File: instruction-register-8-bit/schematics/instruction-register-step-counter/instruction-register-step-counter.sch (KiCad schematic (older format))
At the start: 15 parts

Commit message: small corrections to design
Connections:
- net CLK: no longer U?.2 (CP)
- new net ~CLK: U?.2 (CP)
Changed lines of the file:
@@
 IRi
-Wire Wire Line
-	9825 2300 8675 2300
 Wire Wire Line
 	9825 2500 8575 2500
@@
 Connection ~ 4950 3475
 Wire Wire Line
-	8675 2300 8675 1900
-Wire Wire Line
-	8675 1900 5825 1900
-Wire Wire Line
-	5825 1900 5825 3200
+	8650 1975 5825 1975
+Wire Wire Line
+	5825 1975 5825 3200
 Wire Wire Line
 	5825 3200 4750 3200
 Wire Wire Line
 	4750 3200 4750 3600
-Connection ~ 8675 2300
-Wire Wire Line
-	8675 2300 8575 2300
 $Comp
 L power:GND #PWR?
@@
 	7875 1700 7875 3600
 Connection ~ 2425 1700
+Wire Wire Line
+	8575 2300 9825 2300
+Text HLabel 9825 2100 2    50   Input ~ 0
+~CLK
+Wire Wire Line
+	9825 2100 8650 2100
+Wire Wire Line
+	8650 2100 8650 1975
 $EndSCHEMATC

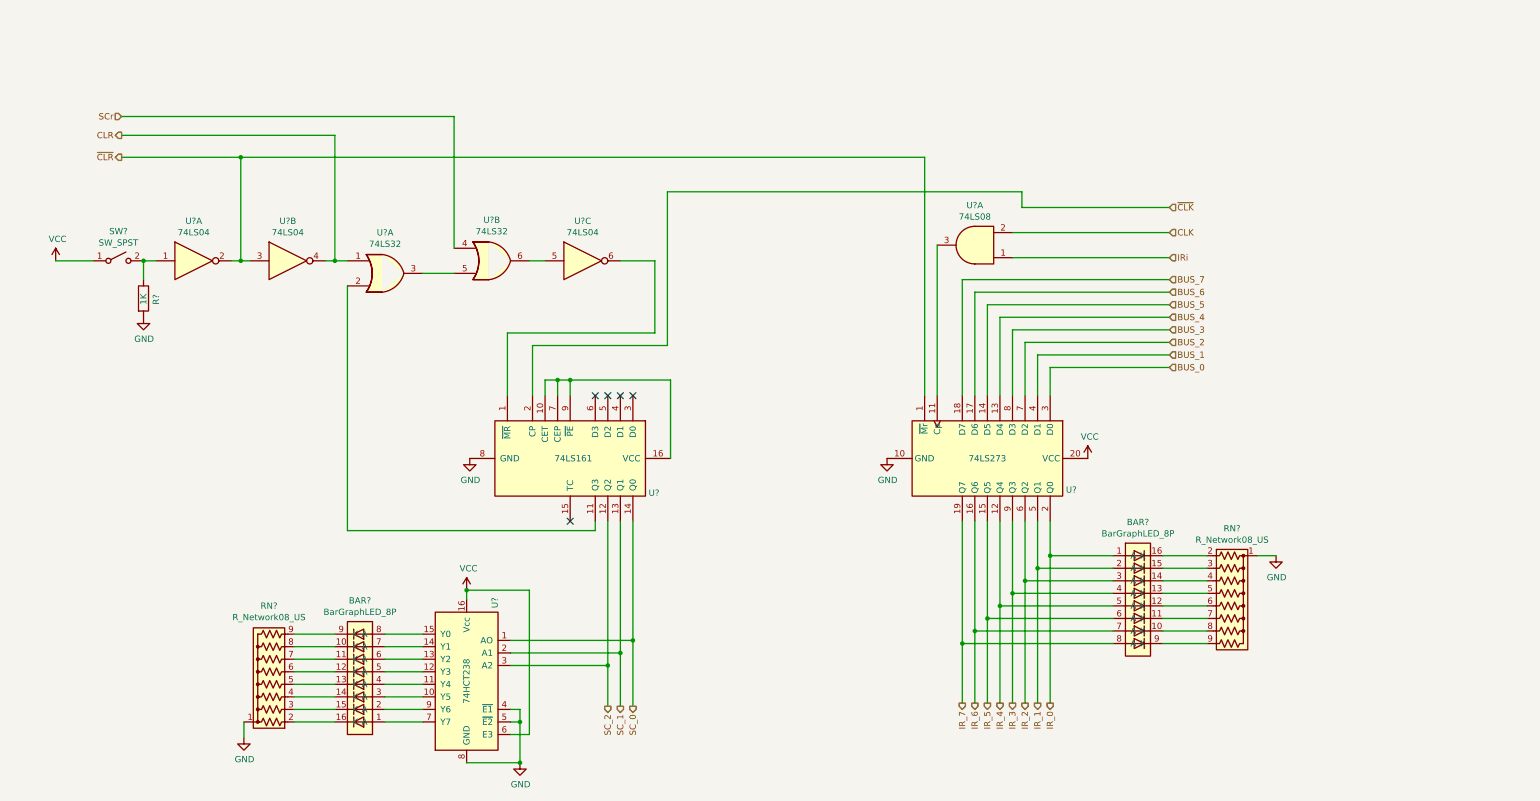
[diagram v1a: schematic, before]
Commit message: updated register design to enable extended instructions
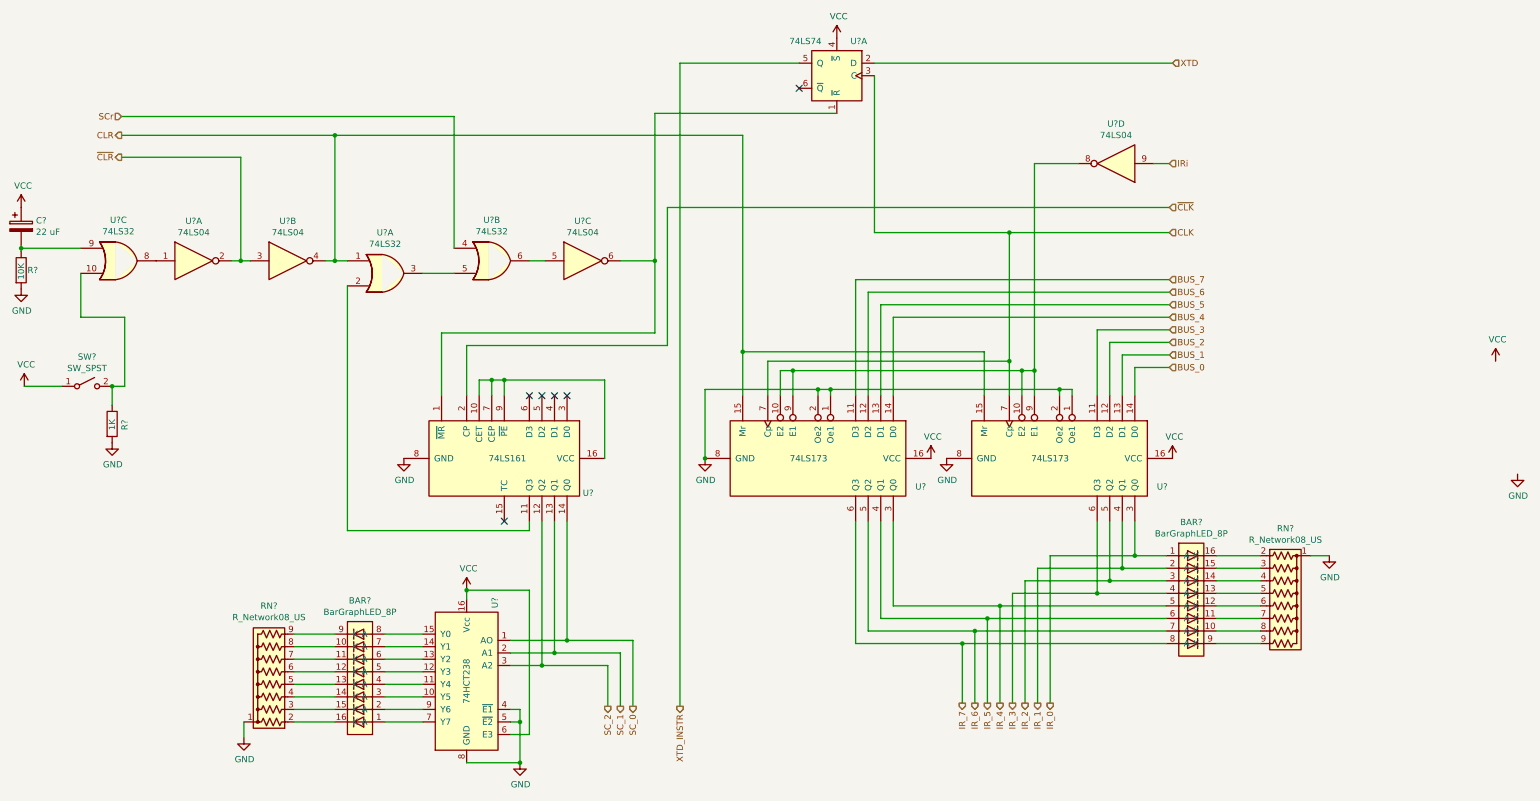
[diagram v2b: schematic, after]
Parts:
- removed U?: 74LS273, symbol 74xx:74LS273
- removed U?: 74LS08, symbol 74xx:74LS08
- added C?: 22 uF, symbol Device:CP
- added R?: 10K, symbol Device:R
- added U? (x2): 74LS173, symbol 74xx:74LS173
- added U?: 74LS74, symbol 74xx:74LS74
- added U?: 74LS04, symbol 74xx:74LS04
- added U?: 74LS32, symbol 74xx:74LS32
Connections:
- net BUS_0: now also U?.14 (D0)
- net BUS_1: now also U?.13 (D1)
- net BUS_2: now also U?.12 (D2)
- net BUS_3: now also U?.11 (D3)
- net BUS_4: now also U?.14 (D0)
- net BUS_5: now also U?.13 (D1)
- net BUS_6: now also U?.12 (D2)
- net BUS_7: now also U?.11 (D3)
- net CLK: now also U?.3 (C), U?.7 (Cp), U?.7 (Cp)
- net CLR: now also U?.15 (Mr), U?.15 (Mr)
- net GND: now also R?.2, U?.1 (Oe1), U?.1 (Oe1), U?.2 (Oe2), U?.2 (Oe2), U?.8 (GND), U?.8 (GND)
- net IR_0: now also U?.3 (Q0)
- net IR_1: now also U?.4 (Q1)
- net IR_2: now also U?.5 (Q2)
- net IR_3: now also U?.6 (Q3)
- net IR_4: now also U?.3 (Q0)
- net IR_5: now also U?.4 (Q1)
- net IR_6: now also U?.5 (Q2)
- net IR_7: now also U?.6 (Q3)
- net IRi: now also U?.9
- net VCC: now also C?.1, U?.16 (VCC), U?.16 (VCC), U?.4 (~S)
- net at U?.1 (~MR), U?.6: now also U?.1 (~R)
- net at R?.1, SW?.2 (B): now also U?.10; no longer U?.1
- new net: U?.1, U?.8
- new net: U?.10 (E2), U?.10 (E2), U?.8, U?.9 (E1), U?.9 (E1)
- new net: C?.2, R?.1, U?.9
- new net XTD: U?.2 (D)
- new net XTD_INSTR: U?.5 (Q)
- no-connect marks 5 -> 6
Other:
- moved on the sheet: BAR?, R?, RN?, SW?, U?

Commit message: candidate final schematic designs
Also started to consolidate custom symbols from all projects
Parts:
- BAR? (x2): symbol instruction-register-symbols:BarGraphLED_8P -> common-symbols:BarGraphLED_8P
- U?: symbol instruction-register-symbols:74HCT238 -> common-symbols:74HCT238
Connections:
- net INSTR_RESET: now reaches U?.5, U?.6
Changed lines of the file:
@@
 IR_7
 $Comp
-L instruction-register-symbols:BarGraphLED_8P BAR?
+L common-symbols:BarGraphLED_8P BAR?
 U 1 1 60CF32C9
 P 10000 5275
@@
 $EndComp
 $Comp
-L instruction-register-symbols:74HCT238 U?
-U 1 1 60D24130
-P 4225 5850
-F 0 "U?" V 4000 6450 50  0000 C CNN
-F 1 "74HCT238" V 4225 5825 50  0000 C CNN
-F 2 "" H 4075 5675 50  0001 C CNN
-F 3 "" H 4075 5675 50  0001 C CNN
-	1    4225 5850
-	-1   0    0    -1
-$EndComp
-$Comp
 L Switch:SW_SPST SW?
 U 1 1 60D2779C
@@
 	5350 5750 5350 6075
 $Comp
-L instruction-register-symbols:BarGraphLED_8P BAR?
+L common-symbols:BarGraphLED_8P BAR?
 U 1 1 60D969A0
 P 3375 5800
@@
 Wire Wire Line
 	2450 6325 2450 6200
-$Comp
-L power:GND #PWR?
-U 1 1 60DE01F3
-P 12600 4225
-F 0 "#PWR?" H 12600 3975 50  0001 C CNN
-F 1 "GND" H 12605 4052 50  0000 C CNN
-F 2 "" H 12600 4225 50  0001 C CNN
-F 3 "" H 12600 4225 50  0001 C CNN
-	1    12600 4225
-	1    0    0    -1
-$EndComp
-$Comp
-L power:VCC #PWR?
-U 1 1 60DE082D
-P 12425 3325
-F 0 "#PWR?" H 12425 3175 50  0001 C CNN
-F 1 "VCC" H 12440 3498 50  0000 C CNN
-F 2 "" H 12425 3325 50  0001 C CNN
-F 3 "" H 12425 3325 50  0001 C CNN
-	1    12425 3325
-	1    0    0    -1
-$EndComp
 Wire Wire Line
 	4575 6200 4650 6200
@@
 $EndComp
 Wire Wire Line
-	4725 2525 4850 2525
+	4725 2525 4775 2525
 Wire Wire Line
 	5725 2525 5725 1350
@@
 Text HLabel 5925 6075 3    50   Output ~ 0
 XTD_INSTR
+$Comp
+L common-symbols:74HCT238 U?
+U 1 1 60D24130
+P 4225 5850
+F 0 "U?" V 4000 6450 50  0000 C CNN
+F 1 "74HCT238" V 4225 5825 50  0000 C CNN
+F 2 "" H 4075 5675 50  0001 C CNN
+F 3 "" H 4075 5675 50  0001 C CNN
+	1    4225 5850
+	-1   0    0    -1
+$EndComp
+Wire Wire Line
+	4775 2525 4775 1225
+Wire Wire Line
+	4775 1225 1475 1225
+Connection ~ 4775 2525
+Wire Wire Line
+	4775 2525 4850 2525
+Text HLabel 1475 1225 0    50   Output ~ 0
+INSTR_RESET
 $EndSCHEMATC

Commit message: removed A16 address line
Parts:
- gave numbers to parts that had none: 15
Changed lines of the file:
@@
 IR_7
 $Comp
-L common-symbols:BarGraphLED_8P BAR?
+L common-symbols:BarGraphLED_8P BAR2
 U 1 1 60CF32C9
 P 10000 5275
-F 0 "BAR?" H 10000 5942 50  0000 C CNN
+F 0 "BAR2" H 10000 5942 50  0000 C CNN
 F 1 "BarGraphLED_8P" H 10000 5851 50  0000 C CNN
 F 2 "" H 10000 5275 50  0001 C CNN
@@
 	8175 5575 8175 6050
 $Comp
-L Device:R_Network08_US RN?
+L Device:R_Network08_US RN2
 U 1 1 60CFC0D8
 P 10750 5275
-F 0 "RN?" V 10133 5275 50  0000 C CNN
+F 0 "RN2" V 10133 5275 50  0000 C CNN
 F 1 "R_Network08_US" V 10224 5275 50  0000 C CNN
 F 2 "Resistor_THT:R_Array_SIP9" V 11225 5275 50  0001 C CNN
@@
 	10200 5575 10550 5575
 $Comp
-L power:GND #PWR?
+L power:GND #PWR014
 U 1 1 60D0AFC0
 P 11100 4875
-F 0 "#PWR?" H 11100 4625 50  0001 C CNN
+F 0 "#PWR014" H 11100 4625 50  0001 C CNN
 F 1 "GND" H 11105 4702 50  0000 C CNN
 F 2 "" H 11100 4875 50  0001 C CNN
@@
 IRi
 $Comp
-L 74xx:74LS161 U?
+L 74xx:74LS161 U4
 U 1 1 60D1A6A2
 P 4525 4100
-F 0 "U?" V 4800 4725 50  0000 L CNN
+F 0 "U4" V 4800 4725 50  0000 L CNN
 F 1 "74LS161" V 4525 3975 50  0000 L CNN
 F 2 "" H 4525 4100 50  0001 C CNN
@@
 $EndComp
 $Comp
-L Switch:SW_SPST SW?
+L Switch:SW_SPST SW1
 U 1 1 60D2779C
 P 1200 3525
-F 0 "SW?" H 1200 3760 50  0000 C CNN
+F 0 "SW1" H 1200 3760 50  0000 C CNN
 F 1 "SW_SPST" H 1200 3669 50  0000 C CNN
 F 2 "" H 1200 3525 50  0001 C CNN
@@
 $EndComp
 $Comp
-L power:VCC #PWR?
+L power:VCC #PWR03
 U 1 1 60D28594
 P 700 3525
-F 0 "#PWR?" H 700 3375 50  0001 C CNN
+F 0 "#PWR03" H 700 3375 50  0001 C CNN
 F 1 "VCC" H 715 3698 50  0000 C CNN
 F 2 "" H 700 3525 50  0001 C CNN
@@
 $EndComp
 $Comp
-L Device:R R?
+L Device:R R2
 U 1 1 60D2896A
 P 1400 3825
-F 0 "R?" V 1500 3775 50  0000 L CNN
+F 0 "R2" V 1500 3775 50  0000 L CNN
 F 1 "1K" V 1400 3775 50  0000 L CNN
 F 2 "" V 1330 3825 50  0001 C CNN
@@
 $EndComp
 $Comp
-L power:GND #PWR?
+L power:GND #PWR04
 U 1 1 60D29CBD
 P 1400 3975
-F 0 "#PWR?" H 1400 3725 50  0001 C CNN
+F 0 "#PWR04" H 1400 3725 50  0001 C CNN
 F 1 "GND" H 1405 3802 50  0000 C CNN
 F 2 "" H 1400 3975 50  0001 C CNN
@@
 	700  3525 1000 3525
 $Comp
-L 74xx:74LS04 U?
+L 74xx:74LS04 U2
 U 1 1 60D2C869
 P 2050 2525
-F 0 "U?" H 2050 2842 50  0000 C CNN
+F 0 "U2" H 2050 2842 50  0000 C CNN
 F 1 "74LS04" H 2050 2751 50  0000 C CNN
 F 2 "" H 2050 2525 50  0001 C CNN
@@
 $EndComp
 $Comp
-L 74xx:74LS32 U?
+L 74xx:74LS32 U1
 U 1 1 60D2EF1E
 P 3575 2625
-F 0 "U?" H 3575 2950 50  0000 C CNN
+F 0 "U1" H 3575 2950 50  0000 C CNN
 F 1 "74LS32" H 3575 2859 50  0000 C CNN
 F 2 "" H 3575 2625 50  0001 C CNN
@@
 $EndComp
 $Comp
-L 74xx:74LS04 U?
+L 74xx:74LS04 U2
 U 2 1 60D358DC
 P 2800 2525
-F 0 "U?" H 2800 2842 50  0000 C CNN
+F 0 "U2" H 2800 2842 50  0000 C CNN
 F 1 "74LS04" H 2800 2751 50  0000 C CNN
 F 2 "" H 2800 2525 50  0001 C CNN
@@
 NoConn ~ 4525 4600
 $Comp
-L 74xx:74LS32 U?
+L 74xx:74LS32 U1
 U 2 1 60D49D1D
 P 4425 2525
-F 0 "U?" H 4425 2850 50  0000 C CNN
+F 0 "U1" H 4425 2850 50  0000 C CNN
 F 1 "74LS32" H 4425 2759 50  0000 C CNN
 F 2 "" H 4425 2525 50  0001 C CNN
@@
 	3875 2625 4125 2625
 $Comp
-L 74xx:74LS04 U?
+L 74xx:74LS04 U2
 U 3 1 60D4E826
 P 5150 2525
-F 0 "U?" H 5150 2842 50  0000 C CNN
+F 0 "U2" H 5150 2842 50  0000 C CNN
 F 1 "74LS04" H 5150 2751 50  0000 C CNN
 F 2 "" H 5150 2525 50  0001 C CNN
@@
 	4225 3200 4225 3600
 $Comp
-L power:GND #PWR?
+L power:GND #PWR06
 U 1 1 60D63CEC
 P 3725 4100
-F 0 "#PWR?" H 3725 3850 50  0001 C CNN
+F 0 "#PWR06" H 3725 3850 50  0001 C CNN
 F 1 "GND" H 3730 3927 50  0000 C CNN
 F 2 "" H 3725 4100 50  0001 C CNN
@@
 	5350 5750 5350 6075
 $Comp
-L common-symbols:BarGraphLED_8P BAR?
+L common-symbols:BarGraphLED_8P BAR1
 U 1 1 60D969A0
 P 3375 5800
-F 0 "BAR?" H 3375 5233 50  0000 C CNN
+F 0 "BAR1" H 3375 5233 50  0000 C CNN
 F 1 "BarGraphLED_8P" H 3375 5324 50  0000 C CNN
 F 2 "" H 3375 5800 50  0001 C CNN
@@
 	3575 6200 3875 6200
 $Comp
-L Device:R_Network08_US RN?
+L Device:R_Network08_US RN1
 U 1 1 60DB642E
 P 2650 5800
-F 0 "RN?" V 3175 5800 50  0000 C CNN
+F 0 "RN1" V 3175 5800 50  0000 C CNN
 F 1 "R_Network08_US" V 3084 5800 50  0000 C CNN
 F 2 "Resistor_THT:R_Array_SIP9" V 3125 5800 50  0001 C CNN
@@
 	2850 6200 3175 6200
 $Comp
-L power:GND #PWR?
+L power:GND #PWR05
 U 1 1 60DDAC2E
 P 2450 6325
-F 0 "#PWR?" H 2450 6075 50  0001 C CNN
+F 0 "#PWR05" H 2450 6075 50  0001 C CNN
 F 1 "GND" H 2455 6152 50  0000 C CNN
 F 2 "" H 2450 6325 50  0001 C CNN
@@
 	4225 5150 4225 5225
 $Comp
-L power:VCC #PWR?
+L power:VCC #PWR07
 U 1 1 60DEFCE4
 P 4225 5150
-F 0 "#PWR?" H 4225 5000 50  0001 C CNN
+F 0 "#PWR07" H 4225 5000 50  0001 C CNN
 F 1 "VCC" H 4240 5323 50  0000 C CNN
 F 2 "" H 4225 5150 50  0001 C CNN
@@
 Connection ~ 4225 5150
 $Comp
-L power:GND #PWR?
+L power:GND #PWR08
 U 1 1 60DF031A
 P 4650 6525
-F 0 "#PWR?" H 4650 6275 50  0001 C CNN
+F 0 "#PWR08" H 4650 6275 50  0001 C CNN
 F 1 "GND" H 4655 6352 50  0000 C CNN
 F 2 "" H 4650 6525 50  0001 C CNN
@@
 ~CLK
 $Comp
-L 74xx:74LS173 U?
+L 74xx:74LS173 U7
 U 1 1 60E06F1E
 P 8950 4100
-F 0 "U?" V 9175 4875 50  0000 L CNN
+F 0 "U7" V 9175 4875 50  0000 L CNN
 F 1 "74LS173" V 8950 3875 50  0000 L CNN
 F 2 "" H 8950 4100 50  0001 C CNN
@@
 $EndComp
 $Comp
-L 74xx:74LS173 U?
+L 74xx:74LS173 U5
 U 1 1 60E0D0CC
 P 7025 4100
-F 0 "U?" V 7250 4875 50  0000 L CNN
+F 0 "U5" V 7250 4875 50  0000 L CNN
 F 1 "74LS173" V 7025 3875 50  0000 L CNN
 F 2 "" H 7025 4100 50  0001 C CNN
@@
 Connection ~ 6425 3250
 $Comp
-L 74xx:74LS04 U?
+L 74xx:74LS04 U2
 U 4 1 60EAE619
 P 9400 1750
-F 0 "U?" H 9400 1433 50  0000 C CNN
+F 0 "U2" H 9400 1433 50  0000 C CNN
 F 1 "74LS04" H 9400 1524 50  0000 C CNN
 F 2 "" H 9400 1750 50  0001 C CNN
@@
 	7125 3550 8950 3550
 $Comp
-L power:GND #PWR?
+L power:GND #PWR09
 U 1 1 60F24388
 P 6125 4100
-F 0 "#PWR?" H 6125 3850 50  0001 C CNN
+F 0 "#PWR09" H 6125 3850 50  0001 C CNN
 F 1 "GND" H 6130 3927 50  0000 C CNN
 F 2 "" H 6125 4100 50  0001 C CNN
@@
 Connection ~ 6125 4100
 $Comp
-L power:GND #PWR?
+L power:GND #PWR012
 U 1 1 60F2496F
 P 8050 4100
-F 0 "#PWR?" H 8050 3850 50  0001 C CNN
+F 0 "#PWR012" H 8050 3850 50  0001 C CNN
 F 1 "GND" H 8055 3927 50  0000 C CNN
 F 2 "" H 8050 4100 50  0001 C CNN
@@
 $EndComp
 $Comp
-L power:VCC #PWR?
+L power:VCC #PWR011
 U 1 1 60F2510D
 P 7925 4100
-F 0 "#PWR?" H 7925 3950 50  0001 C CNN
+F 0 "#PWR011" H 7925 3950 50  0001 C CNN
 F 1 "VCC" H 7940 4273 50  0000 C CNN
 F 2 "" H 7925 4100 50  0001 C CNN
@@
 $EndComp
 $Comp
-L power:VCC #PWR?
+L power:VCC #PWR013
 U 1 1 60F2574C
 P 9850 4100
-F 0 "#PWR?" H 9850 3950 50  0001 C CNN
+F 0 "#PWR013" H 9850 3950 50  0001 C CNN
 F 1 "VCC" H 9865 4273 50  0000 C CNN
 F 2 "" H 9850 4100 50  0001 C CNN
@@
 $EndComp
 $Comp
-L 74xx:74LS32 U?
+L 74xx:74LS32 U1
 U 3 1 60F2D71D
 P 1450 2525
-F 0 "U?" H 1450 2850 50  0000 C CNN
+F 0 "U1" H 1450 2850 50  0000 C CNN
 F 1 "74LS32" H 1450 2759 50  0000 C CNN
 F 2 "" H 1450 2525 50  0001 C CNN
@@
 $EndComp
 $Comp
-L Device:CP C?
+L Device:CP C1
 U 1 1 60F309C4
 P 675 2250
-F 0 "C?" H 793 2296 50  0000 L CNN
+F 0 "C1" H 793 2296 50  0000 L CNN
 F 1 "22 uF" H 793 2205 50  0000 L CNN
 F 2 "" H 713 2100 50  0001 C CNN
@@
 $EndComp
 $Comp
-L Device:R R?
+L Device:R R1
 U 1 1 60F33076
 P 675 2600
-F 0 "R?" H 725 2600 50  0000 L CNN
+F 0 "R1" H 725 2600 50  0000 L CNN
 F 1 "10K" V 675 2525 50  0000 L CNN
 F 2 "" V 605 2600 50  0001 C CNN
@@
 	675  2425 675  2450
 $Comp
-L power:VCC #PWR?
+L power:VCC #PWR01
 U 1 1 60F48D9E
 P 675 2100
-F 0 "#PWR?" H 675 1950 50  0001 C CNN
+F 0 "#PWR01" H 675 1950 50  0001 C CNN
 F 1 "VCC" H 690 2273 50  0000 C CNN
 F 2 "" H 675 2100 50  0001 C CNN
@@
 $EndComp
 $Comp
-L power:GND #PWR?
+L power:GND #PWR02
 U 1 1 60F494BC
 P 675 2750
-F 0 "#PWR?" H 675 2500 50  0001 C CNN
+F 0 "#PWR02" H 675 2500 50  0001 C CNN
 F 1 "GND" H 680 2577 50  0000 C CNN
 F 2 "" H 675 2750 50  0001 C CNN
@@
 	4025 3100 5725 3100
 $Comp
-L 74xx:74LS74 U?
+L 74xx:74LS74 U6
 U 1 1 60E828E3
 P 7175 1050
-F 0 "U?" H 7000 1325 50  0000 C CNN
+F 0 "U6" H 7000 1325 50  0000 C CNN
 F 1 "74LS74" H 7425 1325 50  0000 C CNN
 F 2 "" H 7175 1050 50  0001 C CNN
@@
 NoConn ~ 6875 1150
 $Comp
-L power:VCC #PWR?
+L power:VCC #PWR010
 U 1 1 60EFFFD1
 P 7175 750
-F 0 "#PWR?" H 7175 600 50  0001 C CNN
+F 0 "#PWR010" H 7175 600 50  0001 C CNN
 F 1 "VCC" H 7190 923 50  0000 C CNN
 F 2 "" H 7175 750 50  0001 C CNN
@@
 XTD_INSTR
 $Comp
-L common-symbols:74HCT238 U?
+L common-symbols:74HCT238 U3
 U 1 1 60D24130
 P 4225 5850
-F 0 "U?" V 4000 6450 50  0000 C CNN
+F 0 "U3" V 4000 6450 50  0000 C CNN
 F 1 "74HCT238" V 4225 5825 50  0000 C CNN
 F 2 "" H 4075 5675 50  0001 C CNN

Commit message: tweaks and fixes
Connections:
- net CLR: now also U1.4; no longer U1.1
- net INSTR_RESET: now also U1.8, U2.9; no longer U1.6, U2.5
- net IRi: now also U2.11; no longer U2.9
- net SCr: now also U1.10; no longer U1.4
- net at U4.1 (~MR), U6.1 (~R): now also U2.8; no longer U2.6
- net at U4.11 (Q3): now also U1.5; no longer U1.2
- net at R2.1, SW1.2 (B): now also U1.2; no longer U1.10
- net at U2.1: now also U1.3; no longer U1.8
- net at U5.10 (E2), U5.9 (E1), U7.10 (E2)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: now also U2.10; no longer U2.8
- net at C1.2, R1.1: now also U1.1; no longer U1.9
- new net: U1.6, U1.9
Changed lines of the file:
@@
 $Comp
 L 74xx:74LS32 U1
-U 1 1 60D2EF1E
+U 2 1 60D2EF1E
 P 3575 2625
 F 0 "U1" H 3575 2950 50  0000 C CNN
@@
 F 2 "" H 3575 2625 50  0001 C CNN
 F 3 "http://www.ti.com/lit/gpn/sn74LS32" H 3575 2625 50  0001 C CNN
-	1    3575 2625
+	2    3575 2625
 	1    0    0    -1
 $EndComp
@@
 $Comp
 L 74xx:74LS32 U1
-U 2 1 60D49D1D
+U 3 1 60D49D1D
 P 4425 2525
 F 0 "U1" H 4425 2850 50  0000 C CNN
@@
 F 2 "" H 4425 2525 50  0001 C CNN
 F 3 "http://www.ti.com/lit/gpn/sn74LS32" H 4425 2525 50  0001 C CNN
-	2    4425 2525
-	1    0    0    -1
+	3    4425 2525
+	1    0    0    1
 $EndComp
 Wire Wire Line
@@
 $Comp
 L 74xx:74LS04 U2
-U 3 1 60D4E826
+U 4 1 60D4E826
 P 5150 2525
 F 0 "U2" H 5150 2842 50  0000 C CNN
@@
 F 2 "" H 5150 2525 50  0001 C CNN
 F 3 "http://www.ti.com/lit/gpn/sn74LS04" H 5150 2525 50  0001 C CNN
-	3    5150 2525
+	4    5150 2525
 	1    0    0    -1
 $EndComp
@@
 $Comp
 L 74xx:74LS04 U2
-U 4 1 60EAE619
+U 5 1 60EAE619
 P 9400 1750
 F 0 "U2" H 9400 1433 50  0000 C CNN
@@
 F 2 "" H 9400 1750 50  0001 C CNN
 F 3 "http://www.ti.com/lit/gpn/sn74LS04" H 9400 1750 50  0001 C CNN
-	4    9400 1750
+	5    9400 1750
 	-1   0    0    1
 $EndComp
@@
 $Comp
 L 74xx:74LS32 U1
-U 3 1 60F2D71D
+U 1 1 60F2D71D
 P 1450 2525
 F 0 "U1" H 1450 2850 50  0000 C CNN
@@
 F 2 "" H 1450 2525 50  0001 C CNN
 F 3 "http://www.ti.com/lit/gpn/sn74LS32" H 1450 2525 50  0001 C CNN
-	3    1450 2525
-	1    0    0    -1
-$EndComp
+	1    1450 2525
+	1    0    0    -1
+$EndComp

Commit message: fixed hardware bug with the XTD flip flop
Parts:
- added U8: 74LS08, symbol 74xx:74LS08
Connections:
- net CLK: now also U8.1; no longer U6.3 (C)
- net XTD: now also U8.2
- new net: U6.3 (C), U8.3
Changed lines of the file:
@@
 Connection ~ 5725 2525
 Wire Wire Line
-	7475 1050 7475 2300
-Wire Wire Line
-	7475 2300 8550 2300
-Connection ~ 8550 2300
+	7475 1050 7475 1400
 Wire Wire Line
 	8550 2300 9825 2300
 Wire Wire Line
-	7475 950  9850 950
+	7475 950  8075 950
 Text HLabel 9850 950  2    50   Input ~ 0
 XTD
@@
 Text HLabel 1475 1225 0    50   Output ~ 0
 INSTR_RESET
+$Comp
+L 74xx:74LS08 U8
+U 1 1 612B04C7
+P 7775 1400
+F 0 "U8" H 7775 1083 50  0000 C CNN
+F 1 "74LS08" H 7775 1174 50  0000 C CNN
+F 2 "" H 7775 1400 50  0001 C CNN
+F 3 "http://www.ti.com/lit/gpn/sn74LS08" H 7775 1400 50  0001 C CNN
+	1    7775 1400
+	-1   0    0    1
+$EndComp
+Wire Wire Line
+	8550 2300 8075 2300
+Wire Wire Line
+	8075 2300 8075 1500
+Connection ~ 8550 2300
+Wire Wire Line
+	8075 950  8075 1300
+Connection ~ 8075 950
+Wire Wire Line
+	8075 950  9850 950
 $EndSCHEMATC
